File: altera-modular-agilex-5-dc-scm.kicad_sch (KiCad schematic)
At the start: 6 parts

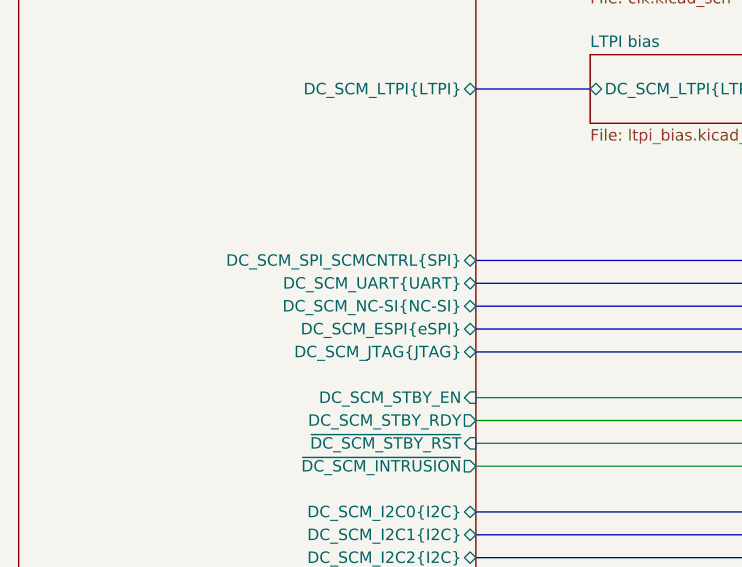
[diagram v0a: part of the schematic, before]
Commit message: [#100501] Move UART level shifter from DC-SCM to HVIO schematic sheet
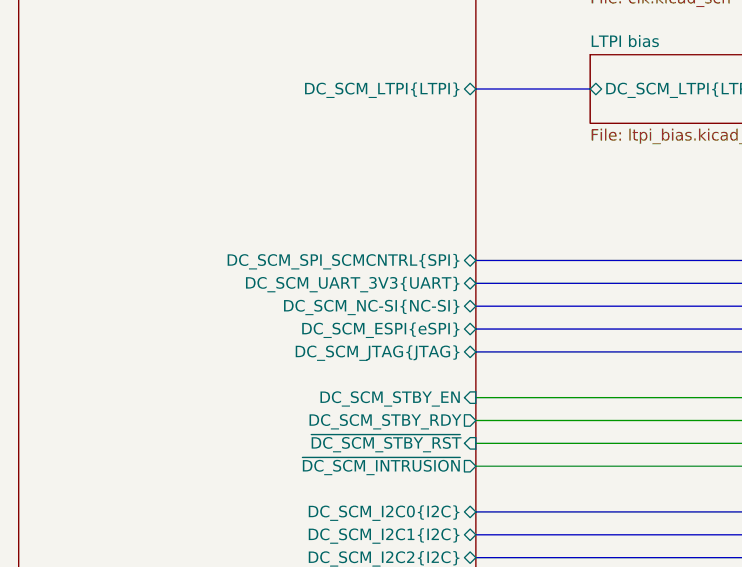
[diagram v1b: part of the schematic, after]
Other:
- sheet DC-SCM 2.1 connector ports: added DC_SCM_UART_3V3{UART}; removed DC_SCM_UART{UART}
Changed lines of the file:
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@@
-			)
-		)
-		(pin "DC_SCM_UART{UART}" bidirectional
-			(at 76.2 119.38 0)
-			(effects
-				(font
-					(size 1.27 1.27)
-				)
-				(justify right)
 			)
 		)
@@
 			(effects
 				(font
+					(size 1.27 1.27)
+				)
+				(justify right)
+			)
+		)
+		(pin "DC_SCM_UART_3V3{UART}" bidirectional
+			(at 76.2 119.38 0)
+			(effects
+				(font

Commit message: [#100501] Gate GbE_PHY_RESET with COLD_RESET signal, to reset ETH PHY
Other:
- sheet ETH PHY ports: added ~{COLD_RESET}, ~{GbE_PHY_RESET}; removed ~{GbE_RESET}
- sheet MitySOM Config ports: added ~{HPS_COLD_RESET}; removed ~{RESET_BTN}
- sheet MitySOM HPS ports: added ~{GbE_PHY_RESET}; removed ~{GbE_RESET}
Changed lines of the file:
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@@
 		(color 0 0 0 0)
 	)
+	(junction
+		(at 261.62 261.62)
+		(diameter 0)
+		(color 0 0 0 0)
+	)
 	(no_connect
 		(at 342.9 43.18)
@@
 		)
 	)
+	(wire
+		(pts
+			(xy 261.62 261.62) (xy 271.78 261.62)
+		)
+		(stroke
+			(width 0)
+			(type default)
+		)
+	)
 	(bus
 		(pts
@@
 	(wire
 		(pts
-			(xy 271.78 134.62) (xy 271.78 149.86)
+			(xy 271.78 134.62) (xy 271.78 142.24)
 		)
 		(stroke
@@
 		)
 	)
+	(wire
+		(pts
+			(xy 304.8 149.86) (xy 261.62 149.86)
+		)
+		(stroke
+			(width 0)
+			(type default)
+		)
+	)
 	(bus
 		(pts
@@
 	(wire
 		(pts
-			(xy 271.78 149.86) (xy 304.8 149.86)
+			(xy 271.78 142.24) (xy 304.8 142.24)
 		)
 		(stroke
@@
 	(wire
 		(pts
-			(xy 241.3 261.62) (xy 271.78 261.62)
+			(xy 241.3 261.62) (xy 261.62 261.62)
 		)
 		(stroke
@@
 	(wire
 		(pts
+			(xy 261.62 149.86) (xy 261.62 261.62)
+		)
+		(stroke
+			(width 0)
+			(type default)
+		)
+	)
+	(wire
+		(pts
 			(xy 246.38 254) (xy 246.38 241.3)
 		)
@@
 			)
 		)
-		(pin "~{GbE_RESET}" output
+		(pin "~{GbE_PHY_RESET}" output
 			(at 254 134.62 0)
 			(effects
@@
 			)
 		)
-		(pin "~{RESET_BTN}" input
-			(at 241.3 261.62 0)
+		(pin "~{CONFIG_BTN}" input
+			(at 241.3 264.16 0)
 			(effects
 				(font
@@
 			)
 		)
-		(pin "~{CONFIG_BTN}" input
-			(at 241.3 264.16 0)
+		(pin "SDM{JTAG}" input
+			(at 241.3 256.54 0)
 			(effects
 				(font
@@
 			)
 		)
-		(pin "SDM{JTAG}" input
-			(at 241.3 256.54 0)
+		(pin "~{HPS_COLD_RESET}" input
+			(at 241.3 261.62 0)
 			(effects
 				(font
@@
 			)
 		)
-		(pin "~{GbE_RESET}" input
+		(pin "~{COLD_RESET}" input
 			(at 304.8 149.86 180)
 			(effects
 				(font
+					(size 1.27 1.27)
+				)
+				(justify left)
+			)
+		)
+		(pin "~{GbE_PHY_RESET}" input
+			(at 304.8 142.24 180)
+			(effects
+				(font

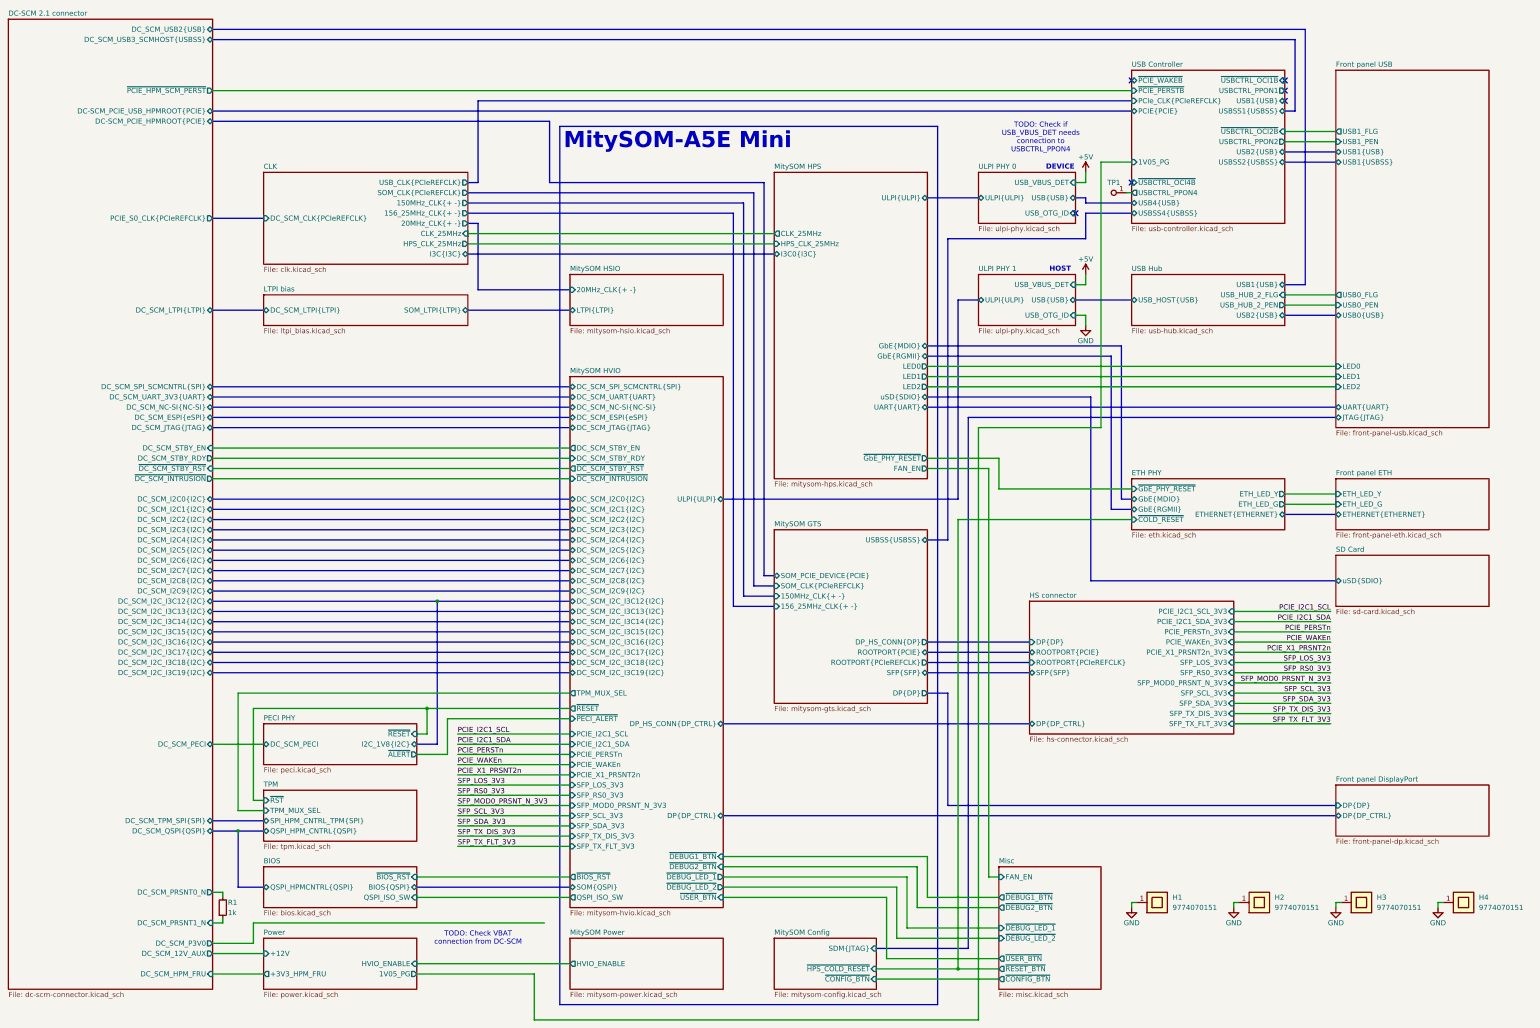
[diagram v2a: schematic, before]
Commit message: [#100501] Add Tag-Connect to JTAG and config EEPROM to FTDI, connect DC-SCM USB1 to USB controller
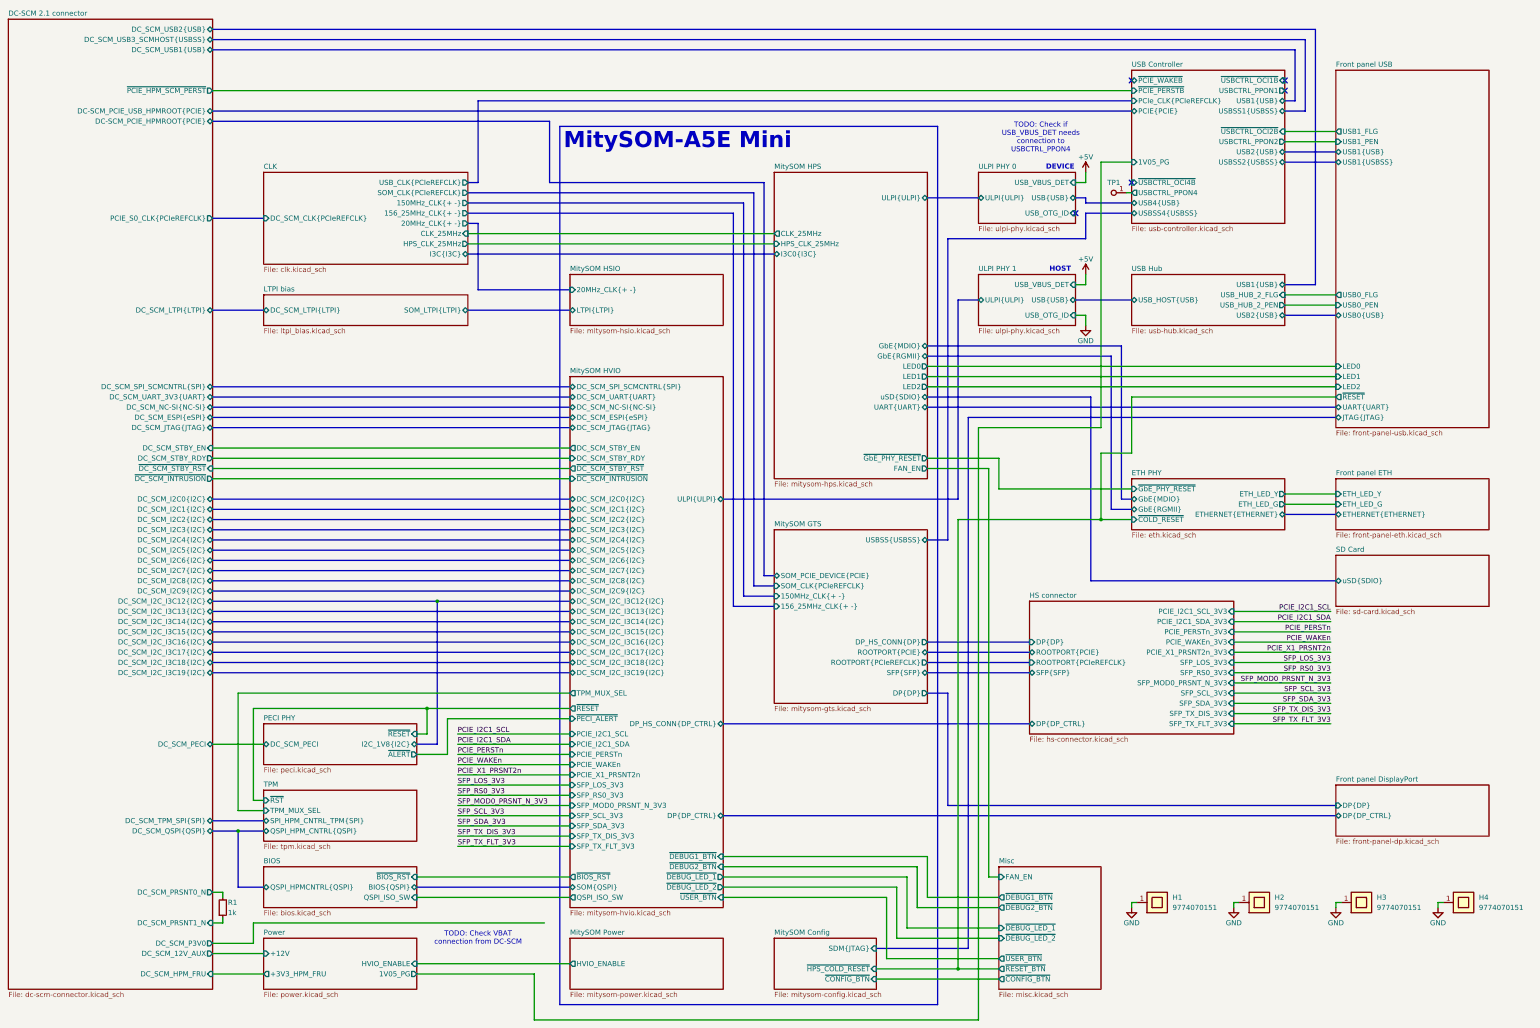
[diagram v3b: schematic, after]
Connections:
- no-connect marks 6 -> 5
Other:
- sheet DC-SCM 2.1 connector ports: added DC_SCM_USB1{USB}; removed none
- sheet Front panel USB ports: added ~{RESET}; removed none
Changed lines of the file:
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@@
 	)
 	(junction
+		(at 297.18 149.86)
+		(diameter 0)
+		(color 0 0 0 0)
+	)
+	(junction
 		(at 132.08 170.18)
 		(diameter 0)
@@
 	)
 	(no_connect
-		(at 342.9 45.72)
-	)
-	(no_connect
 		(at 342.9 40.64)
 	)
@@
 		)
 	)
+	(wire
+		(pts
+			(xy 304.8 119.38) (xy 304.8 133.35)
+		)
+		(stroke
+			(width 0)
+			(type default)
+		)
+	)
 	(bus
 		(pts
@@
 		)
 	)
+	(bus
+		(pts
+			(xy 345.44 33.02) (xy 345.44 45.72)
+		)
+		(stroke
+			(width 0)
+			(type default)
+		)
+	)
 	(wire
 		(pts
@@
 	(bus
 		(pts
-			(xy 342.9 48.26) (xy 345.44 48.26)
+			(xy 342.9 48.26) (xy 347.98 48.26)
 		)
 		(stroke
@@
 	(wire
 		(pts
+			(xy 297.18 133.35) (xy 297.18 149.86)
+		)
+		(stroke
+			(width 0)
+			(type default)
+		)
+	)
+	(wire
+		(pts
 			(xy 76.2 139.7) (xy 165.1 139.7)
 		)
@@
 		)
 	)
+	(wire
+		(pts
+			(xy 355.6 119.38) (xy 304.8 119.38)
+		)
+		(stroke
+			(width 0)
+			(type default)
+		)
+	)
 	(bus
 		(pts
@@
 	(bus
 		(pts
+			(xy 342.9 45.72) (xy 345.44 45.72)
+		)
+		(stroke
+			(width 0)
+			(type default)
+		)
+	)
+	(bus
+		(pts
 			(xy 142.24 45.72) (xy 304.8 45.72)
 		)
@@
 	(bus
 		(pts
-			(xy 345.44 30.48) (xy 345.44 48.26)
+			(xy 347.98 30.48) (xy 347.98 48.26)
 		)
 		(stroke
@@
 		)
 	)
+	(wire
+		(pts
+			(xy 297.18 149.86) (xy 261.62 149.86)
+		)
+		(stroke
+			(width 0)
+			(type default)
+		)
+	)
 	(bus
 		(pts
@@
 	(bus
 		(pts
-			(xy 76.2 27.94) (xy 347.98 27.94)
+			(xy 76.2 27.94) (xy 350.52 27.94)
 		)
 		(stroke
@@
 	(bus
 		(pts
-			(xy 347.98 91.44) (xy 347.98 27.94)
+			(xy 350.52 91.44) (xy 350.52 27.94)
 		)
 		(stroke
@@
 	(wire
 		(pts
-			(xy 304.8 149.86) (xy 261.62 149.86)
+			(xy 304.8 149.86) (xy 297.18 149.86)
 		)
 		(stroke
@@
 	(bus
 		(pts
-			(xy 342.9 91.44) (xy 347.98 91.44)
+			(xy 342.9 91.44) (xy 350.52 91.44)
 		)
 		(stroke
@@
 	(bus
 		(pts
-			(xy 76.2 30.48) (xy 345.44 30.48)
+			(xy 76.2 30.48) (xy 347.98 30.48)
 		)
 		(stroke
@@
 	(wire
 		(pts
+			(xy 304.8 133.35) (xy 297.18 133.35)
+		)
+		(stroke
+			(width 0)
+			(type default)
+		)
+	)
+	(wire
+		(pts
 			(xy 139.7 78.74) (xy 215.9 78.74)
 		)
@@
 		)
 	)
+	(bus
+		(pts
+			(xy 76.2 33.02) (xy 345.44 33.02)
+		)
+		(stroke
+			(width 0)
+			(type default)
+		)
+	)
 	(wire
 		(pts
@@
 			)
 		)
+		(pin "DC_SCM_USB1{USB}" bidirectional
+			(at 76.2 33.02 0)
+			(effects
+				(font
+					(size 1.27 1.27)
+				)
+				(justify right)
+			)
+		)
 		(instances
 			(project "altera-modular-agilex-5-dc-scm"
@@
 			(effects
 				(font
+					(size 1.27 1.27)
+				)
+				(justify left)
+			)
+		)
+		(pin "~{RESET}" output
+			(at 355.6 119.38 180)
+			(effects
+				(font

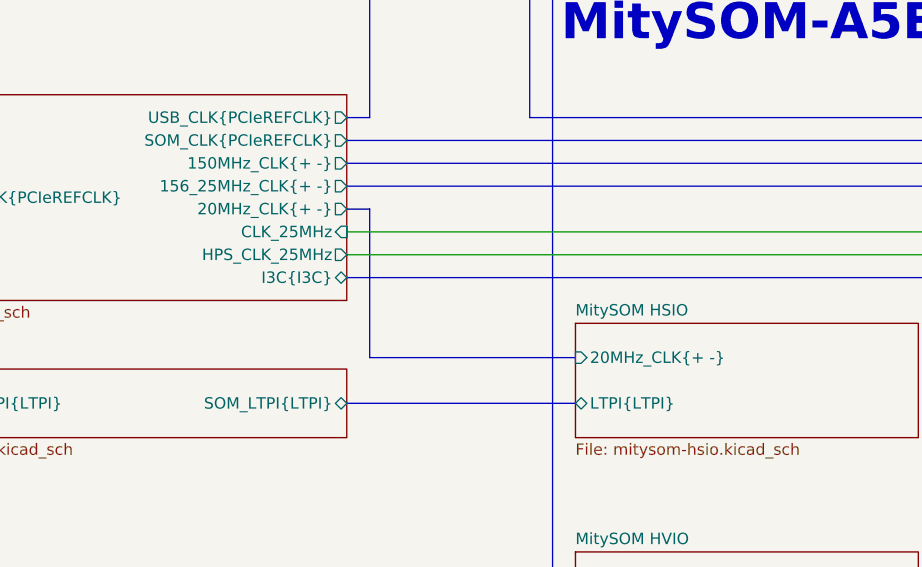
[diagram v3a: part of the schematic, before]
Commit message: [#100501] Add ferrite bead to CLK gen supply, change its decoupling from 1uF to 100nF, rename 20MHz bus to 25MHz
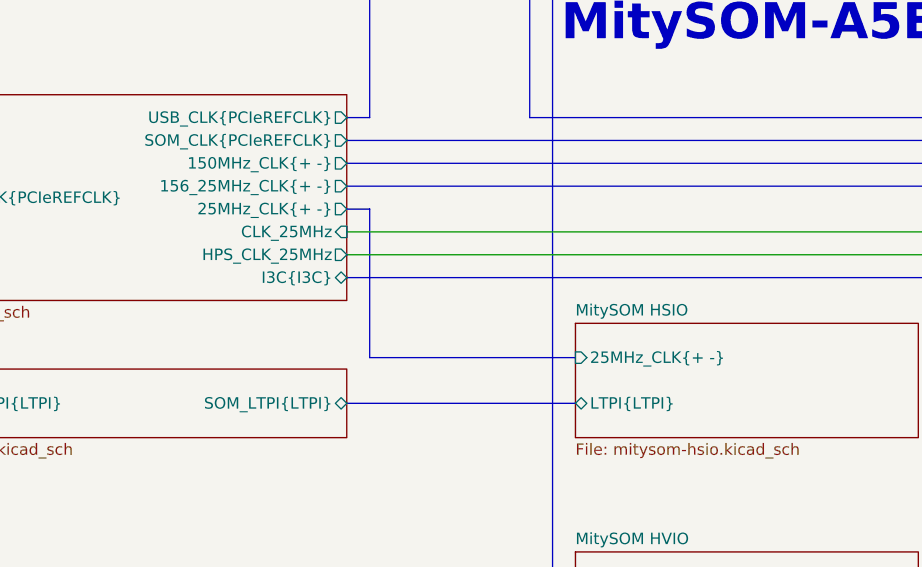
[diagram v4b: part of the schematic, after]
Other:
- sheet CLK ports: added 25MHz_CLK{+ -}; removed 20MHz_CLK{+ -}
- sheet MitySOM HSIO ports: added 25MHz_CLK{+ -}; removed 20MHz_CLK{+ -}
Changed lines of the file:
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@@
 			)
 		)
-		(pin "20MHz_CLK{+ -}" input
+		(pin "25MHz_CLK{+ -}" input
 			(at 165.1 92.71 180)
 			(effects
@@
 			)
 		)
-		(pin "20MHz_CLK{+ -}" output
-			(at 139.7 76.2 0)
-			(effects
-				(font
-					(size 1.27 1.27)
-				)
-				(justify right)
-			)
-		)
 		(pin "150MHz_CLK{+ -}" output
 			(at 139.7 71.12 0)
@@
 			(effects
 				(font
+					(size 1.27 1.27)
+				)
+				(justify right)
+			)
+		)
+		(pin "25MHz_CLK{+ -}" output
+			(at 139.7 76.2 0)
+			(effects
+				(font

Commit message: [#100501] Improve USB controller schematic readability
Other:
- sheet USB Controller ports: added ~{PCIE_PERST}, ~{PCIE_WAKE}, ~{USBCTRL_OCI1}, ~{USBCTRL_OCI2}, ~{USBCTRL_OCI4}; removed ~{PCIE_PERSTB}, ~{PCIE_WAKEB}, ~{USBCTRL_OCI1B}, ~{USBCTRL_OCI2B}, ~{USBCTRL_OCI4B}
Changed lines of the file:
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@@
 			)
 		)
-		(pin "~{PCIE_PERSTB}" input
+		(pin "1V05_PG" input
+			(at 304.8 60.96 180)
+			(effects
+				(font
+					(size 1.27 1.27)
+				)
+				(justify left)
+			)
+		)
+		(pin "~{PCIE_PERST}" input
 			(at 304.8 43.18 180)
 			(effects
@@
 			)
 		)
-		(pin "~{PCIE_WAKEB}" bidirectional
+		(pin "~{PCIE_WAKE}" bidirectional
 			(at 304.8 40.64 180)
 			(effects
@@
 			)
 		)
-		(pin "~{USBCTRL_OCI1B}" input
+		(pin "~{USBCTRL_OCI1}" input
 			(at 342.9 40.64 0)
 			(effects
@@
 			)
 		)
-		(pin "~{USBCTRL_OCI2B}" input
+		(pin "~{USBCTRL_OCI2}" input
 			(at 342.9 53.34 0)
 			(effects
@@
 			)
 		)
-		(pin "~{USBCTRL_OCI4B}" input
+		(pin "~{USBCTRL_OCI4}" input
 			(at 304.8 66.04 180)
 			(effects
 				(font
-					(size 1.27 1.27)
-				)
-				(justify left)
-			)
-		)
-		(pin "1V05_PG" input
-			(at 304.8 60.96 180)
-			(effects
-				(font
